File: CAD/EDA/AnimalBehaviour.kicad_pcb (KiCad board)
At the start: 2 copper layers, 106.5 x 83.5 mm, 26 parts, among them J1 SSR_INPUT, J10 JSolenoid, J11 LED, J12 Cam, J13 Imaging, J14 Ext Supp, J2 SSR OUT, J3 StimCurrentInject, J4 StimIsoIN, J5 StimIsoIN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

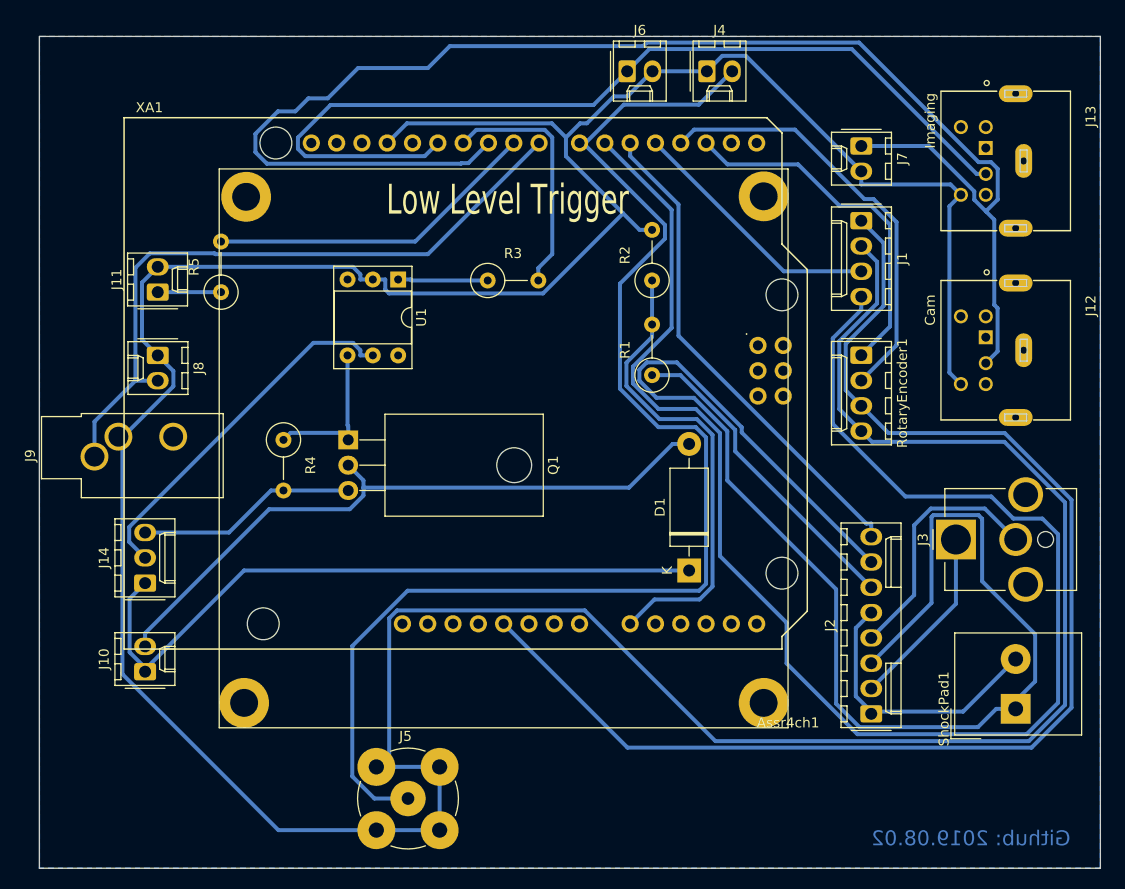
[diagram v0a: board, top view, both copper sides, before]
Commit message: new version. Replace pontentiometer with large R in serial of pin D5.
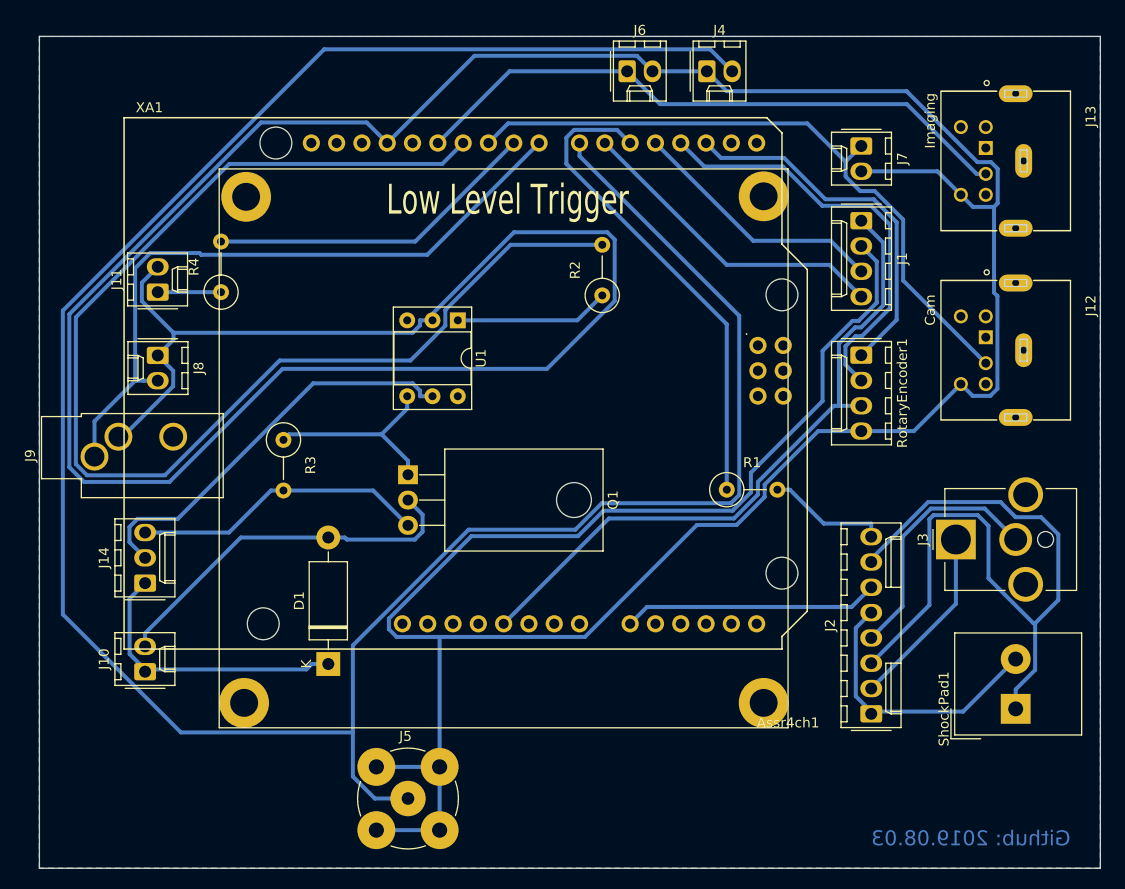
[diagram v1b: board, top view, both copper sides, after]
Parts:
- removed the R2 at (169.0, 89.0)
- R1: value 10K -> 10M
- moved D1 37.4 mm to (136.5, 127.5)
- moved R1 13.7 mm to (176.5, 110.0), turned to 0 degrees
- moved R2 11.6 mm to (164.0, 90.5), turned to 90 degrees
- moved U1 7.26 mm to (149.5, 93.0)
- moved Q1 6.95 mm to (144.5, 108.5)
- renumbered R3 to R2, R4 to R3, R5 to R4
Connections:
- J2 pad 6: ShockReadIn -> ShockRead
- R1 pad 1: ShockReadIn -> Net-(R1-Pad1)
- R1 pad 2: ShockRead -> ShockPWM
- XA1 pad D5: ShockPWM -> Net-(R1-Pad1)
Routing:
- net ShockRelayCh34: track 154.8 -> 32.1 mm
- net ShockStimIsolator: track 131.2 -> 250.1 mm
- net Puff: track 24.8 -> 124.7 mm
- net CamTTL: track 146.8 -> 67.4 mm
- net DGND: track 406.5 -> 483.6 mm
- net 5V: track 131.4 -> 67.4 mm
- net PAD+: track 140.8 -> 77.3 mm
- net Net-(R1-Pad1): track 0.00 -> 49.3 mm
- net EX_12V: track 68.9 -> 28.8 mm
- net ShockPWM: track 49.8 -> 12.1 mm
- net ShockReadIn: track 32.1 -> 0.00 mm
- net ImagingTrig: track 93.9 -> 62.3 mm
- net Net-(D1-Pad2): track 67.2 -> 37.3 mm
- net ShockRead: track 47.4 -> 25.7 mm
- net AGND: track 22.1 -> 29.6 mm
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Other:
- board text added: "Github: 2019.08.03"
- board text removed: "Github: 2019.08.02"
